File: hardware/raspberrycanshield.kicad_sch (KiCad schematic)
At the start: 28 parts, among them J101 I2C, J102 USART

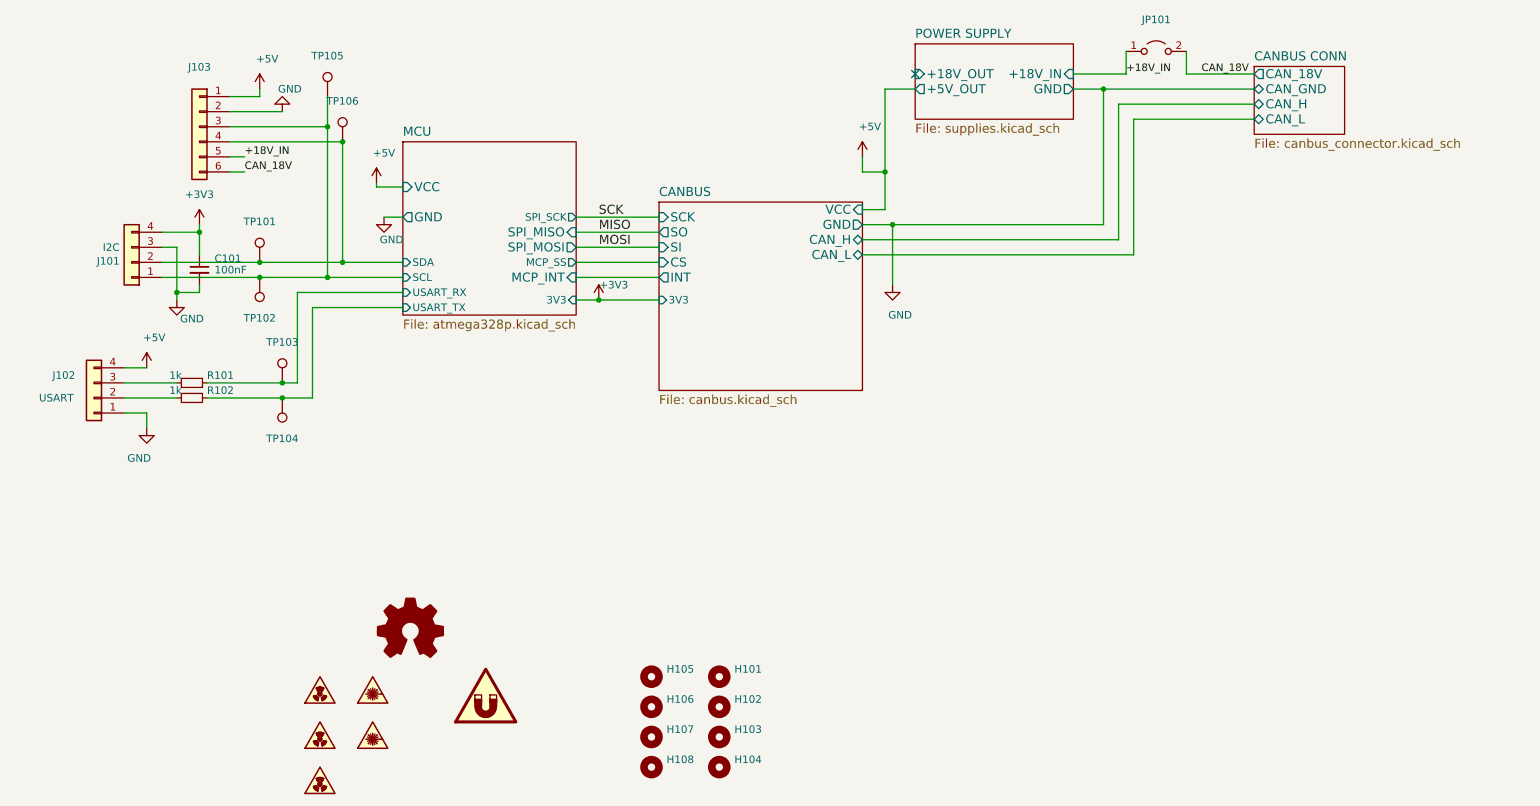
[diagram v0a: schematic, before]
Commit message: hardware: Silkscreen update
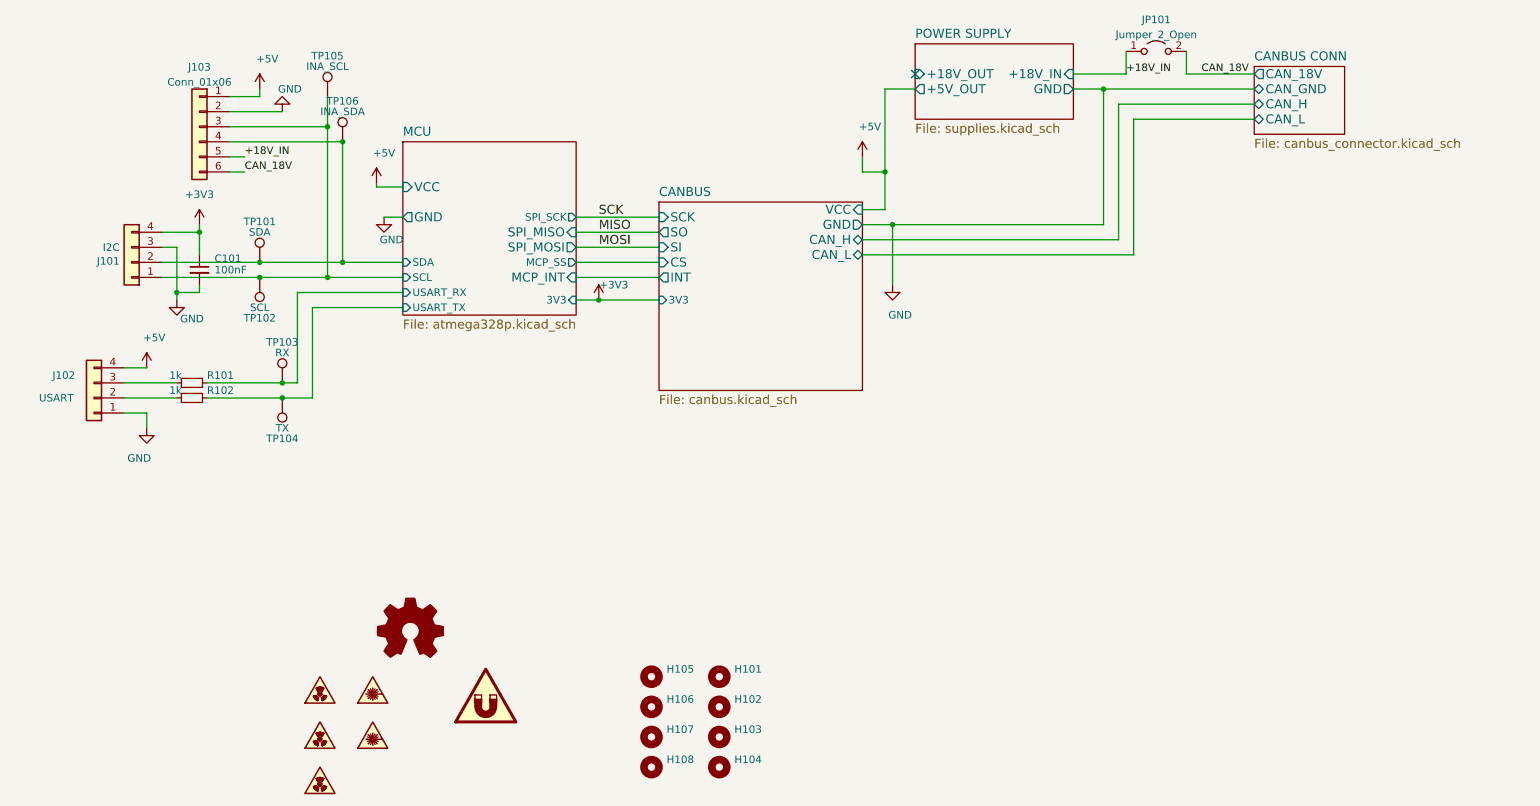
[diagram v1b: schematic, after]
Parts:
- J103: value (none) -> Conn_01x06; footprint (none) -> Connector_PinHeader_2.54mm:PinHeader_1x06_P2.54mm_Vertical
- JP101: value (none) -> Jumper_2_Open; footprint (none) -> Jumper:SolderJumper-2_P1.3mm_Open_RoundedPad1.0x1.5mm
- TP101: value (none) -> SDA; footprint (none) -> TestPoint:TestPoint_Pad_2.0x2.0mm
- TP102: value (none) -> SCL; footprint (none) -> TestPoint:TestPoint_Pad_2.0x2.0mm
- TP103: value (none) -> RX; footprint (none) -> TestPoint:TestPoint_Pad_2.0x2.0mm
- TP104: value (none) -> TX; footprint (none) -> TestPoint:TestPoint_Pad_2.0x2.0mm
- TP105: value (none) -> INA_SCL; footprint (none) -> TestPoint:TestPoint_Pad_2.0x2.0mm
- TP106: value (none) -> INA_SDA; footprint (none) -> TestPoint:TestPoint_Pad_2.0x2.0mm
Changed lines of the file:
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@@
     (in_bom yes) (on_board yes)
     (property "Reference" "TP103" (id 0) (at 71.12 103.632 0))
-    (property "Value" "" (id 1) (at 71.12 105.41 0))
-    (property "Footprint" "" (id 2) (at 76.2 110.49 0)
+    (property "Value" "RX" (id 1) (at 71.12 105.41 0))
+    (property "Footprint" "TestPoint:TestPoint_Pad_2.0x2.0mm" (id 2) (at 76.2 110.49 0)
       (effects (font (size 1.27 1.27)) hide)
     )
@@
     (in_bom yes) (on_board yes)
     (property "Reference" "TP102" (id 0) (at 67.31 99.568 0))
-    (property "Value" "" (id 1) (at 67.31 97.79 0))
-    (property "Footprint" "" (id 2) (at 62.23 92.71 0)
+    (property "Value" "SCL" (id 1) (at 67.31 97.79 0))
+    (property "Footprint" "TestPoint:TestPoint_Pad_2.0x2.0mm" (id 2) (at 62.23 92.71 0)
       (effects (font (size 1.27 1.27)) hide)
     )
@@
     (in_bom yes) (on_board yes) (fields_autoplaced)
     (property "Reference" "JP101" (id 0) (at 218.44 49.2592 0))
-    (property "Value" "" (id 1) (at 218.44 51.7961 0))
-    (property "Footprint" "" (id 2) (at 218.44 54.61 0)
+    (property "Value" "Jumper_2_Open" (id 1) (at 218.44 51.7961 0))
+    (property "Footprint" "Jumper:SolderJumper-2_P1.3mm_Open_RoundedPad1.0x1.5mm" (id 2) (at 218.44 54.61 0)
       (effects (font (size 1.27 1.27)) hide)
     )
@@
     (in_bom yes) (on_board yes)
     (property "Reference" "TP104" (id 0) (at 71.12 119.888 0))
-    (property "Value" "" (id 1) (at 71.12 118.11 0))
-    (property "Footprint" "" (id 2) (at 66.04 113.03 0)
+    (property "Value" "TX" (id 1) (at 71.12 118.11 0))
+    (property "Footprint" "TestPoint:TestPoint_Pad_2.0x2.0mm" (id 2) (at 66.04 113.03 0)
       (effects (font (size 1.27 1.27)) hide)
     )
@@
     (in_bom yes) (on_board yes)
     (property "Reference" "TP106" (id 0) (at 81.28 62.992 0))
-    (property "Value" "" (id 1) (at 81.28 64.77 0))
-    (property "Footprint" "" (id 2) (at 86.36 69.85 0)
+    (property "Value" "INA_SDA" (id 1) (at 81.28 64.77 0))
+    (property "Footprint" "TestPoint:TestPoint_Pad_2.0x2.0mm" (id 2) (at 86.36 69.85 0)
       (effects (font (size 1.27 1.27)) hide)
     )
@@
     (in_bom yes) (on_board yes) (fields_autoplaced)
     (property "Reference" "J103" (id 0) (at 57.15 57.2602 0))
-    (property "Value" "" (id 1) (at 57.15 59.7971 0))
-    (property "Footprint" "" (id 2) (at 57.15 67.31 0)
+    (property "Value" "Conn_01x06" (id 1) (at 57.15 59.7971 0))
+    (property "Footprint" "Connector_PinHeader_2.54mm:PinHeader_1x06_P2.54mm_Vertical" (id 2) (at 57.15 67.31 0)
       (effects (font (size 1.27 1.27)) hide)
     )
@@
     (in_bom yes) (on_board yes)
     (property "Reference" "TP105" (id 0) (at 78.74 55.372 0))
-    (property "Value" "" (id 1) (at 78.74 57.15 0))
-    (property "Footprint" "" (id 2) (at 83.82 62.23 0)
+    (property "Value" "INA_SCL" (id 1) (at 78.74 57.15 0))
+    (property "Footprint" "TestPoint:TestPoint_Pad_2.0x2.0mm" (id 2) (at 83.82 62.23 0)
       (effects (font (size 1.27 1.27)) hide)
     )
@@
     (in_bom yes) (on_board yes)
     (property "Reference" "TP101" (id 0) (at 67.31 83.312 0))
-    (property "Value" "" (id 1) (at 67.31 85.09 0))
-    (property "Footprint" "" (id 2) (at 72.39 90.17 0)
-      (effects (font (size 1.27 1.27)) hide)
-    )
+    (property "Value" "SDA" (id 1) (at 67.31 85.09 0))
+    (property "Footprint" "TestPoint:TestPoint_Pad_2.0x2.0mm" (id 2) (at 72.39 90.17 0)
+      (effects (font (size 1.27 1.27)) hide)
+    )

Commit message: Silkscreen updated with JLC. Finished.
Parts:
- added R103, R104: (no value), symbol Device:R_Small
- R101: value 1k -> (none); footprint Resistor_SMD:R_0603_1608Metric_Pad0.98x0.95mm_HandSolder -> (none)
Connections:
- net +3V3: now also R103.1, R104.1
- net MCU/SCL: now also R104.2
- net MCU/SDA: now also R103.2
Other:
- moved on the sheet: C101, J101
